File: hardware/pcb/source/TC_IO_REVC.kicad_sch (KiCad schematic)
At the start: 71 parts, among them J1 WIRE_PADS_NO_COMPONENT, J10 WIRE_PADS_NO_COMPONENT, J11 WIRE_PADS_NO_COMPONENT, J12 WIRE_PADS_NO_COMPONENT, J13 WIRE_PADS_NO_COMPONENT, J14 WIRE_PADS_NO_COMPONENT, J2 WIRE_PADS_NO_COMPONENT, J3 WIRE_PADS_NO_COMPONENT, J4 WIRE_PADS_NO_COMPONENT, J5 WIRE_PADS_NO_COMPONENT, J6 WIRE_PADS_NO_COMPONENT, J7 WIRE_PADS_NO_COMPONENT, J8 WIRE_PADS_NO_COMPONENT, J9 WIRE_PADS_NO_COMPONENT, U1 MCP3008T-I/SL, U2 SN74HC221DR, U3 SN74HC221DR, U4 SN74HC08DR, U5 SN74HC08DR, U6 SN74HC08DR, U7 MCP100T-300I/TT

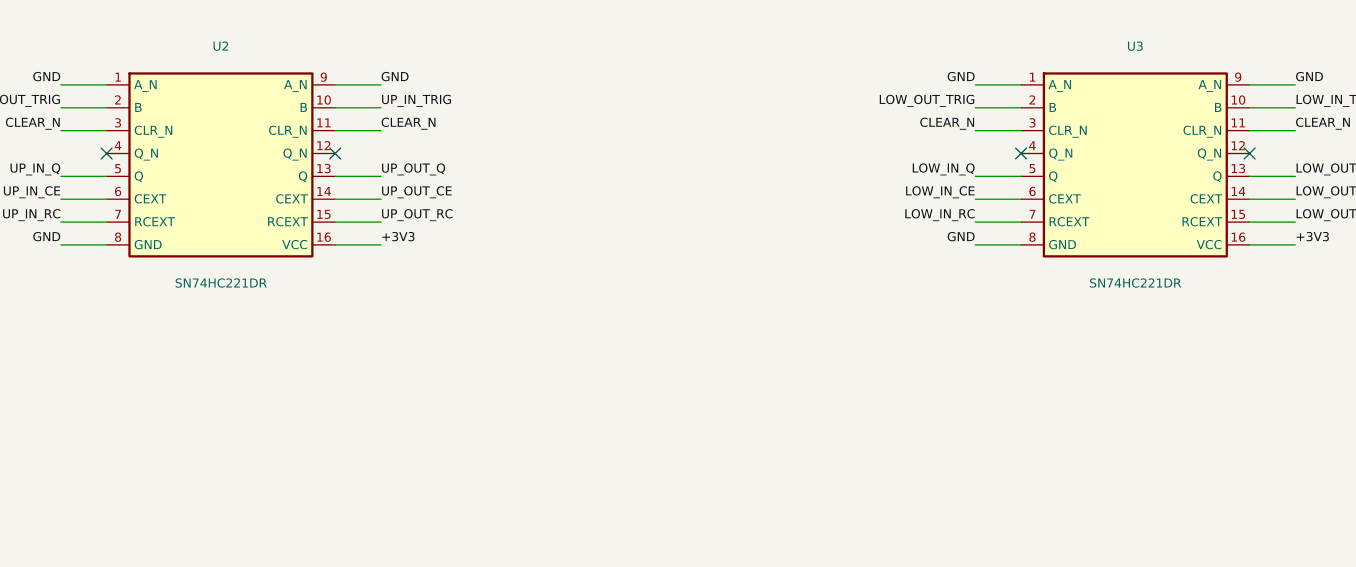
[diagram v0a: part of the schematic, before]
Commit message: Replace one-shot ICs with CD74HC221M96 C133954 and refresh review outputs
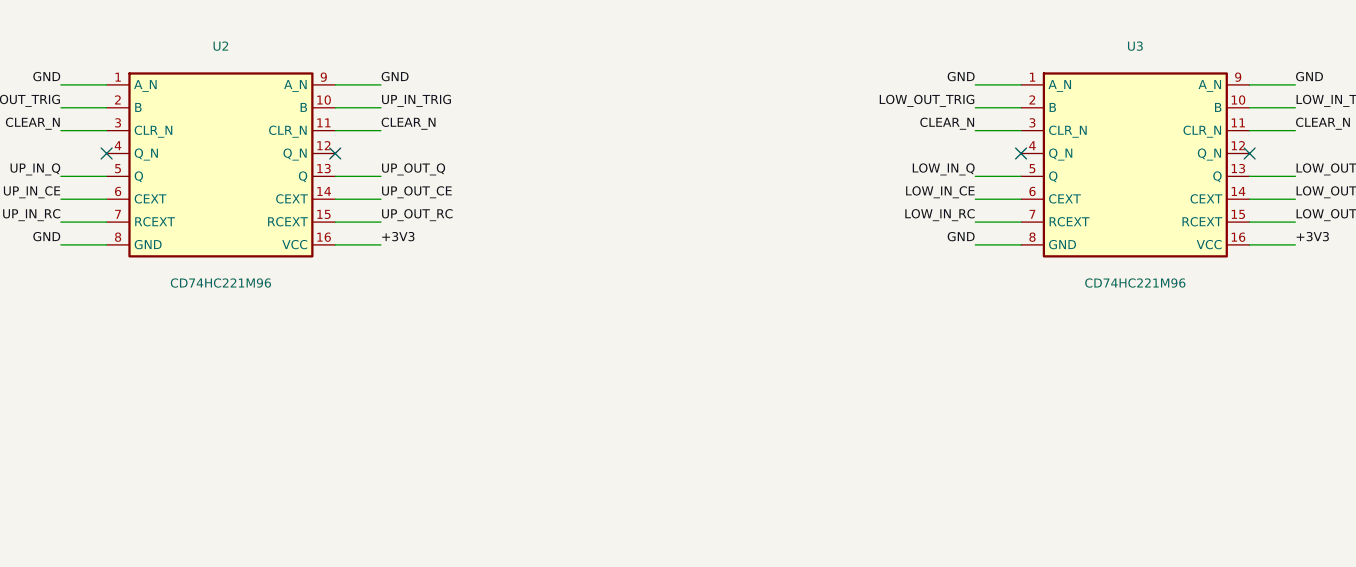
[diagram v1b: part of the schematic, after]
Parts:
- U2, U3: value SN74HC221DR -> CD74HC221M96
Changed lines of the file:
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@@
 (symbol (lib_id "TC:U2") (at 355.59999999999997 127.0 0) (unit 1) (in_bom yes) (on_board yes) (dnp no)
 (property "Reference" "U2" (at 355.59999999999997 113.84 0) (effects (font (size 1 1))))
-(property "Value" "SN74HC221DR" (at 355.59999999999997 140.16 0) (effects (font (size 1 1))))
+(property "Value" "CD74HC221M96" (at 355.59999999999997 140.16 0) (effects (font (size 1 1))))
 (property "Footprint" "Package_SO:SOIC-16_3.9x9.9mm_P1.27mm" (at 355.59999999999997 127.0 0) (effects (font (size 1 1)) (hide yes)))
 (pin "1")
@@
 (symbol (lib_id "TC:U3") (at 457.2 127.0 0) (unit 1) (in_bom yes) (on_board yes) (dnp no)
 (property "Reference" "U3" (at 457.2 113.84 0) (effects (font (size 1 1))))
-(property "Value" "SN74HC221DR" (at 457.2 140.16 0) (effects (font (size 1 1))))
+(property "Value" "CD74HC221M96" (at 457.2 140.16 0) (effects (font (size 1 1))))
 (property "Footprint" "Package_SO:SOIC-16_3.9x9.9mm_P1.27mm" (at 457.2 127.0 0) (effects (font (size 1 1)) (hide yes)))
 (pin "1")

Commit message: Adopt C2167387 timing capacitors with user accepted approximate timing
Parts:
- C1, C2, C3, C4: value 470nF_5%_X7R_50V -> 470nF_10%_X7R_50V
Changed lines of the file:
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@@
 (symbol (lib_id "TC:C1") (at 50.8 431.8 0) (unit 1) (in_bom yes) (on_board yes) (dnp no)
 (property "Reference" "C1" (at 50.8 426.26 0) (effects (font (size 1 1))))
-(property "Value" "470nF_5%_X7R_50V" (at 50.8 437.34000000000003 0) (effects (font (size 1 1))))
+(property "Value" "470nF_10%_X7R_50V" (at 50.8 437.34000000000003 0) (effects (font (size 1 1))))
 (property "Footprint" "Capacitor_SMD:C_1206_3216Metric" (at 50.8 431.8 0) (effects (font (size 1 1)) (hide yes)))
 (pin "1")
@@
 (symbol (lib_id "TC:C2") (at 355.59999999999997 431.8 0) (unit 1) (in_bom yes) (on_board yes) (dnp no)
 (property "Reference" "C2" (at 355.59999999999997 426.26 0) (effects (font (size 1 1))))
-(property "Value" "470nF_5%_X7R_50V" (at 355.59999999999997 437.34000000000003 0) (effects (font (size 1 1))))
+(property "Value" "470nF_10%_X7R_50V" (at 355.59999999999997 437.34000000000003 0) (effects (font (size 1 1))))
 (property "Footprint" "Capacitor_SMD:C_1206_3216Metric" (at 355.59999999999997 431.8 0) (effects (font (size 1 1)) (hide yes)))
 (pin "1")
@@
 (symbol (lib_id "TC:C3") (at 660.3999999999999 431.8 0) (unit 1) (in_bom yes) (on_board yes) (dnp no)
 (property "Reference" "C3" (at 660.3999999999999 426.26 0) (effects (font (size 1 1))))
-(property "Value" "470nF_5%_X7R_50V" (at 660.3999999999999 437.34000000000003 0) (effects (font (size 1 1))))
+(property "Value" "470nF_10%_X7R_50V" (at 660.3999999999999 437.34000000000003 0) (effects (font (size 1 1))))
 (property "Footprint" "Capacitor_SMD:C_1206_3216Metric" (at 660.3999999999999 431.8 0) (effects (font (size 1 1)) (hide yes)))
 (pin "1")
@@
 (symbol (lib_id "TC:C4") (at 152.39999999999998 508.00000000000006 0) (unit 1) (in_bom yes) (on_board yes) (dnp no)
 (property "Reference" "C4" (at 152.39999999999998 502.46000000000004 0) (effects (font (size 1 1))))
-(property "Value" "470nF_5%_X7R_50V" (at 152.39999999999998 513.5400000000001 0) (effects (font (size 1 1))))
+(property "Value" "470nF_10%_X7R_50V" (at 152.39999999999998 513.5400000000001 0) (effects (font (size 1 1))))
 (property "Footprint" "Capacitor_SMD:C_1206_3216Metric" (at 152.39999999999998 508.00000000000006 0) (effects (font (size 1 1)) (hide yes)))
 (pin "1")
